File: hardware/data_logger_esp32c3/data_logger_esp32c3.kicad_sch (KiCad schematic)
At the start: 8 parts, among them J1 USB_C_Receptacle_USB2.0, U1 ESP32-C3-MINI-1

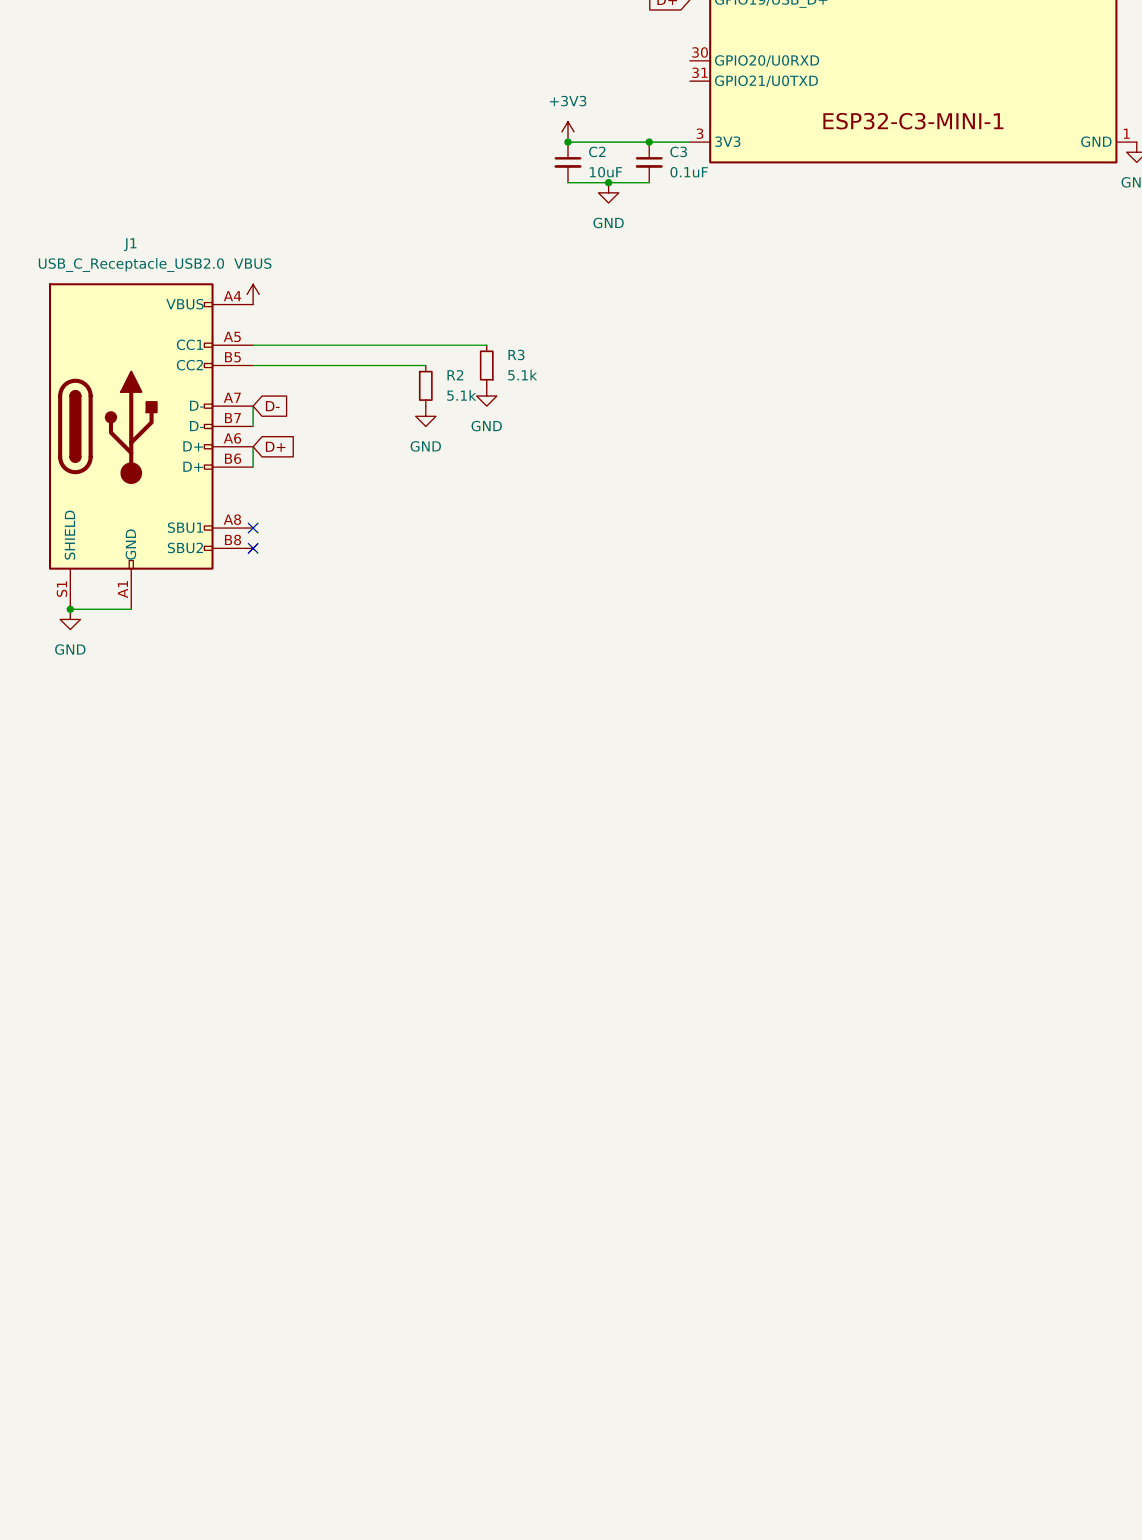
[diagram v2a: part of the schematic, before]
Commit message: Added regulator circuit
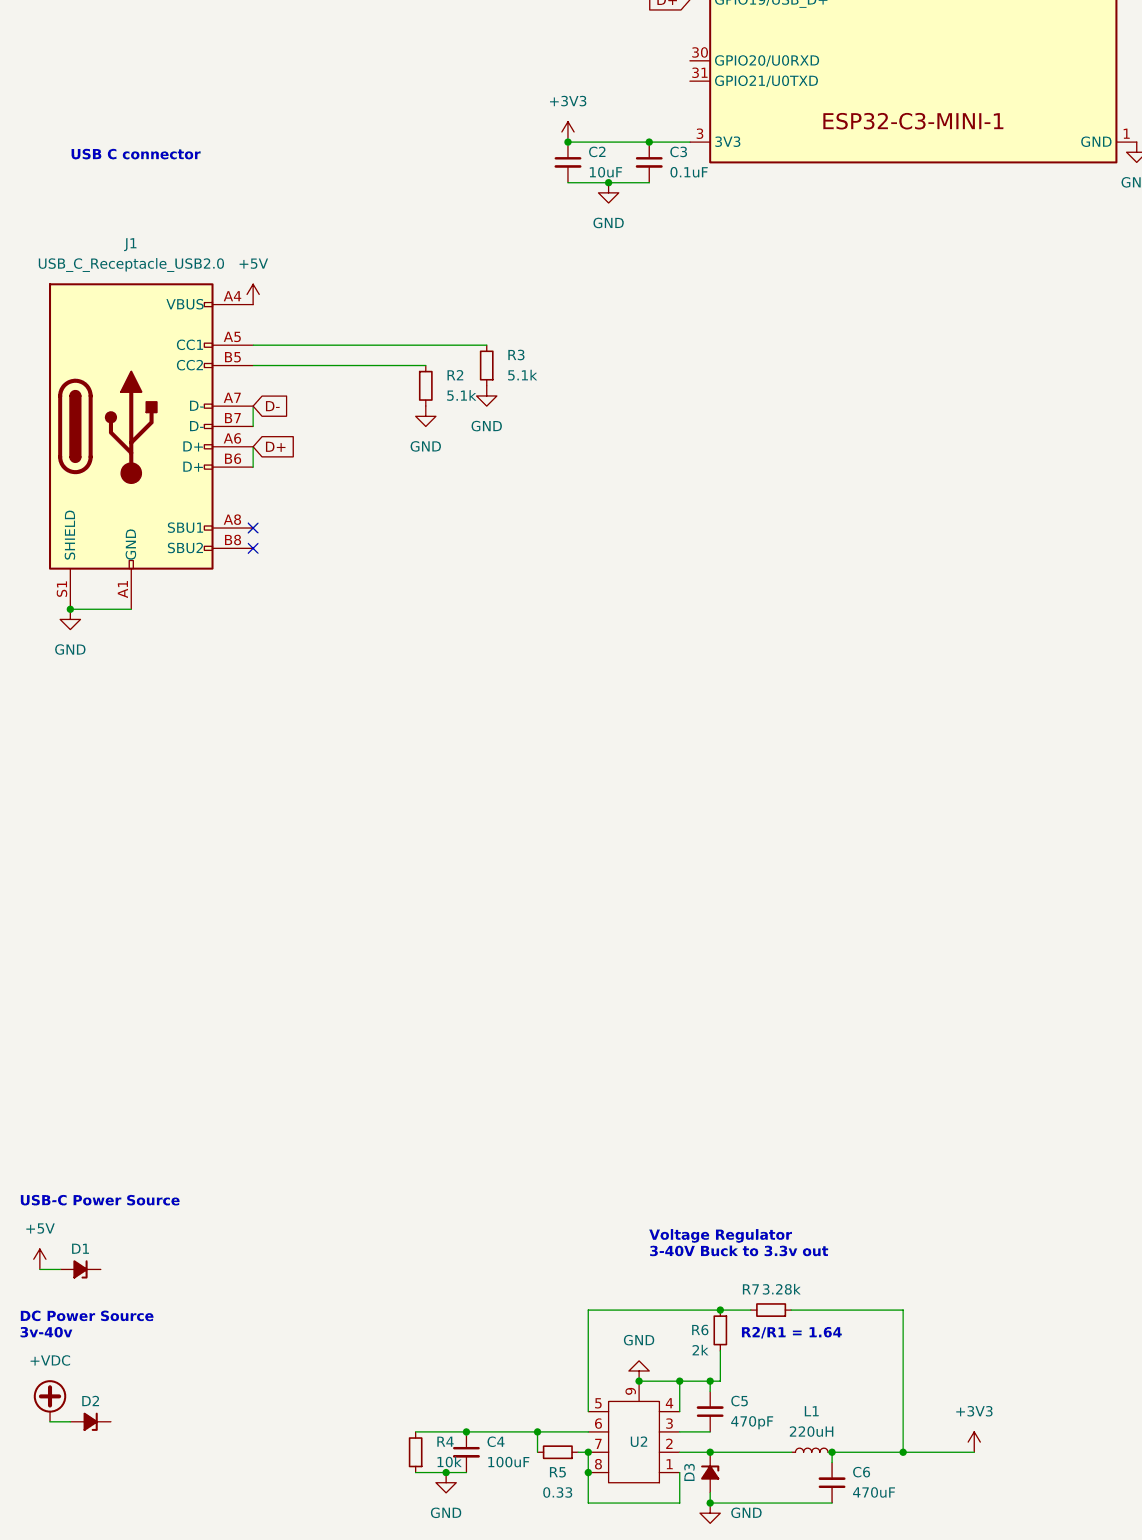
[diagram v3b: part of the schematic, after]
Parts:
- added C4: 100uF, Capacitor_SMD:C_0603_1608Metric, symbol Device:C_Small
- added C5: 470pF, Capacitor_SMD:C_0603_1608Metric, symbol Device:C_Small
- added C6: 470uF, Capacitor_SMD:C_0603_1608Metric, symbol Device:C_Small
- added D1, D2, D3: D_Zener_Small_Filled, Diode_SMD:D_0603_1608Metric, symbol Device:D_Zener_Small_Filled
- added L1: 220uH, Inductor_SMD:L_6.3x6.3_H3, symbol Device:L_Small
- added R4: 10k, Resistor_SMD:R_0603_1608Metric, symbol Device:R_Small
- added R5: 0.33, Resistor_SMD:R_0603_1608Metric, symbol Device:R_Small
- added R6: 2k, Resistor_SMD:R_0603_1608Metric, symbol Device:R_Small
- added R7: 3.28k, Resistor_SMD:R_0603_1608Metric, symbol Device:R_Small
- added U2: MC34063ADRJR, lib:8-WDFN Exposed Pad, symbol lib:MC34063ADRJR
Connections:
- net +3V3: now also C6.2, L1.2, R7.1
- net GND: now also C4.2, C5.2, C6.1, D3.2 (A), R4.1, R6.2, U2.4 (gnd), U2.9 (thermal_pad)
- net VBUS renamed +5V
- net +5V: now also D1.2 (A)
- new net: C4.1, R4.2, R5.2, U2.6 (Vcc)
- new net: R5.1, U2.1 (switch_collector), U2.7 (Ipk), U2.8 (drive_collector)
- new net: D3.1 (K), L1.1, U2.2 (switch_emitter)
- new net: C5.1, U2.3 (timing_cap)
- new net: R6.1, R7.2, U2.5 (comparitor_inverting_input)
- new net +VDC: D2.2 (A)
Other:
- note added: "DC Power Source 3v-40v"
- note added: "R2/R1 = 1.64"
- note added: "USB C connector"
- note added: "USB-C Power Source"
- note added: "Voltage Regulator 3-40V Buck to 3.3v out"

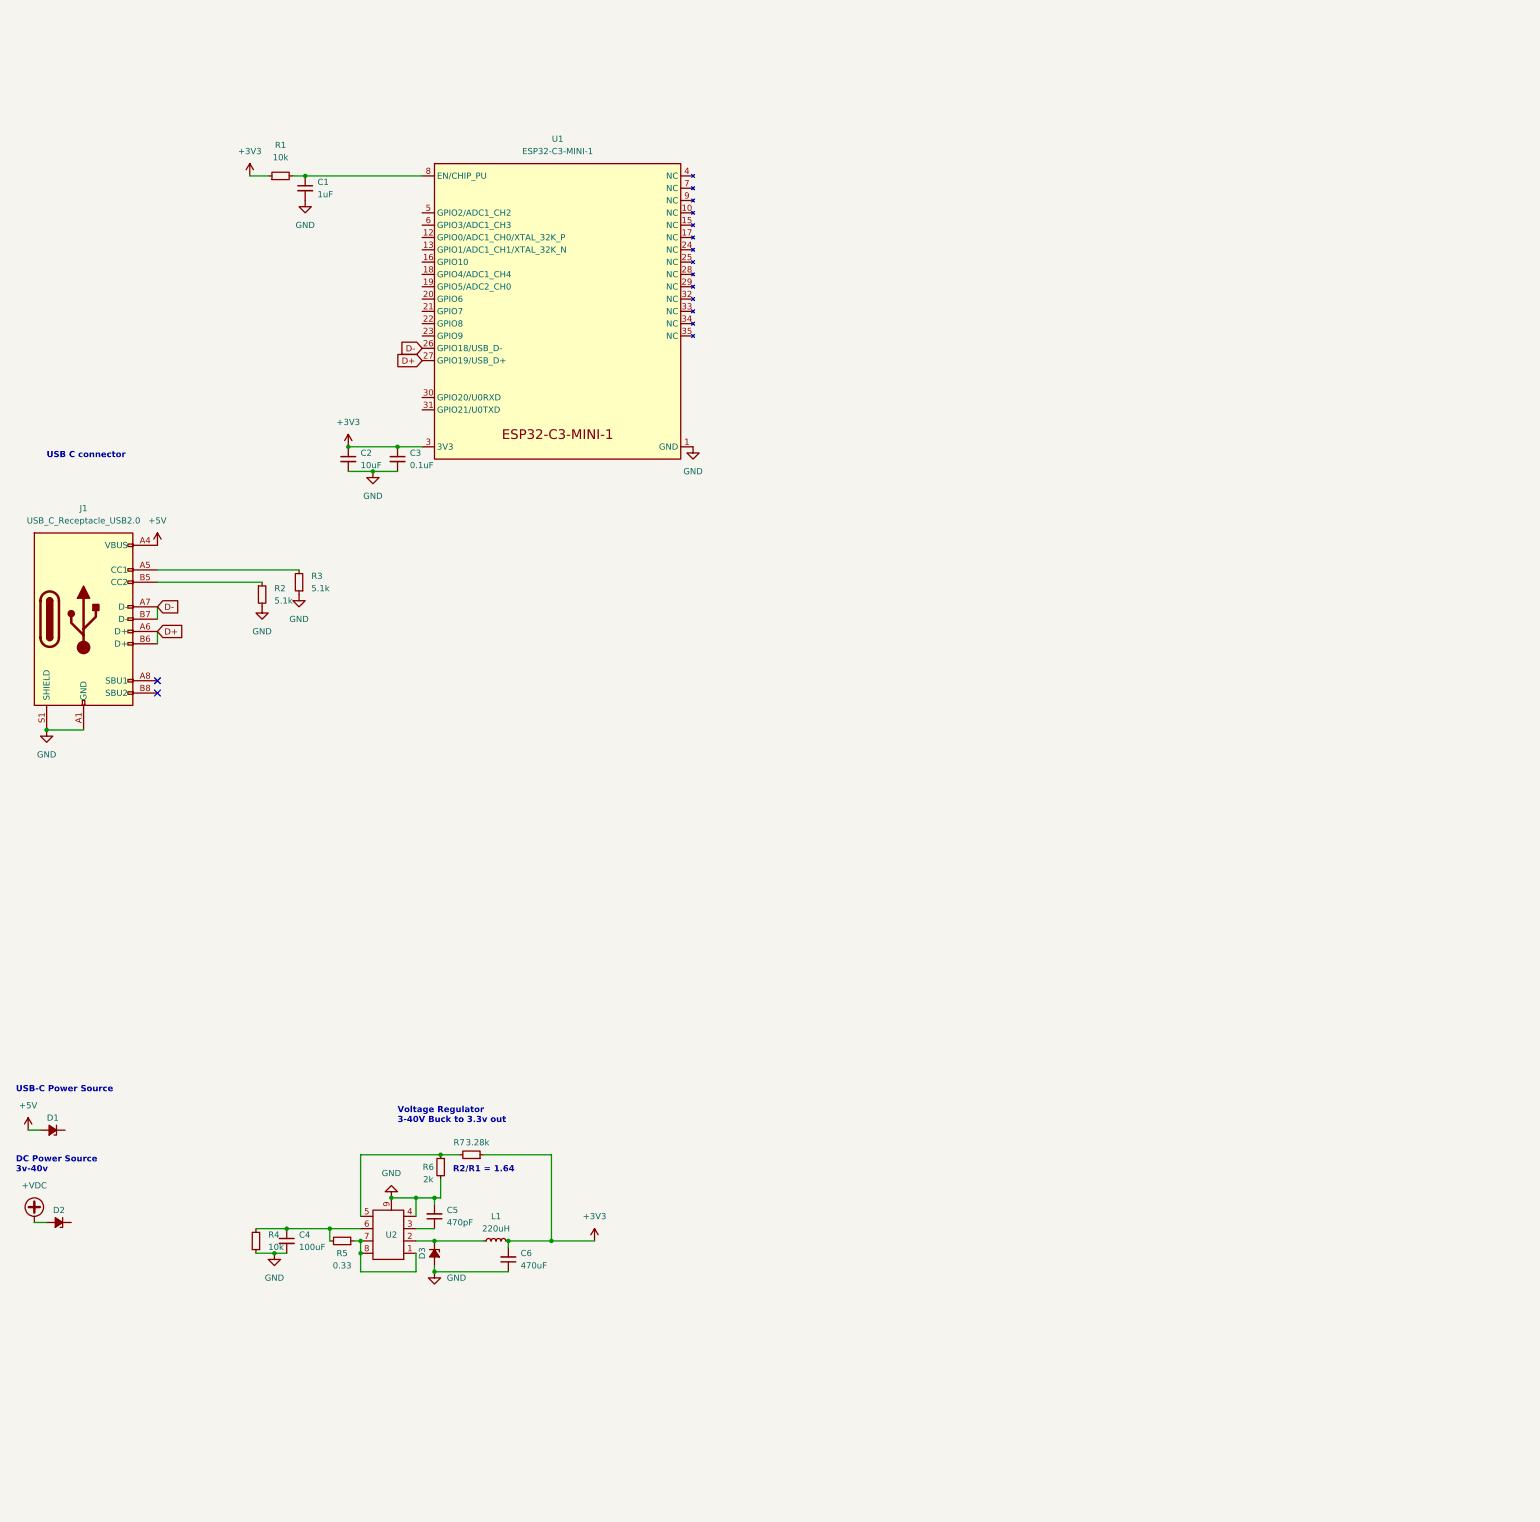
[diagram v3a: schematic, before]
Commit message: Added uSD circuit
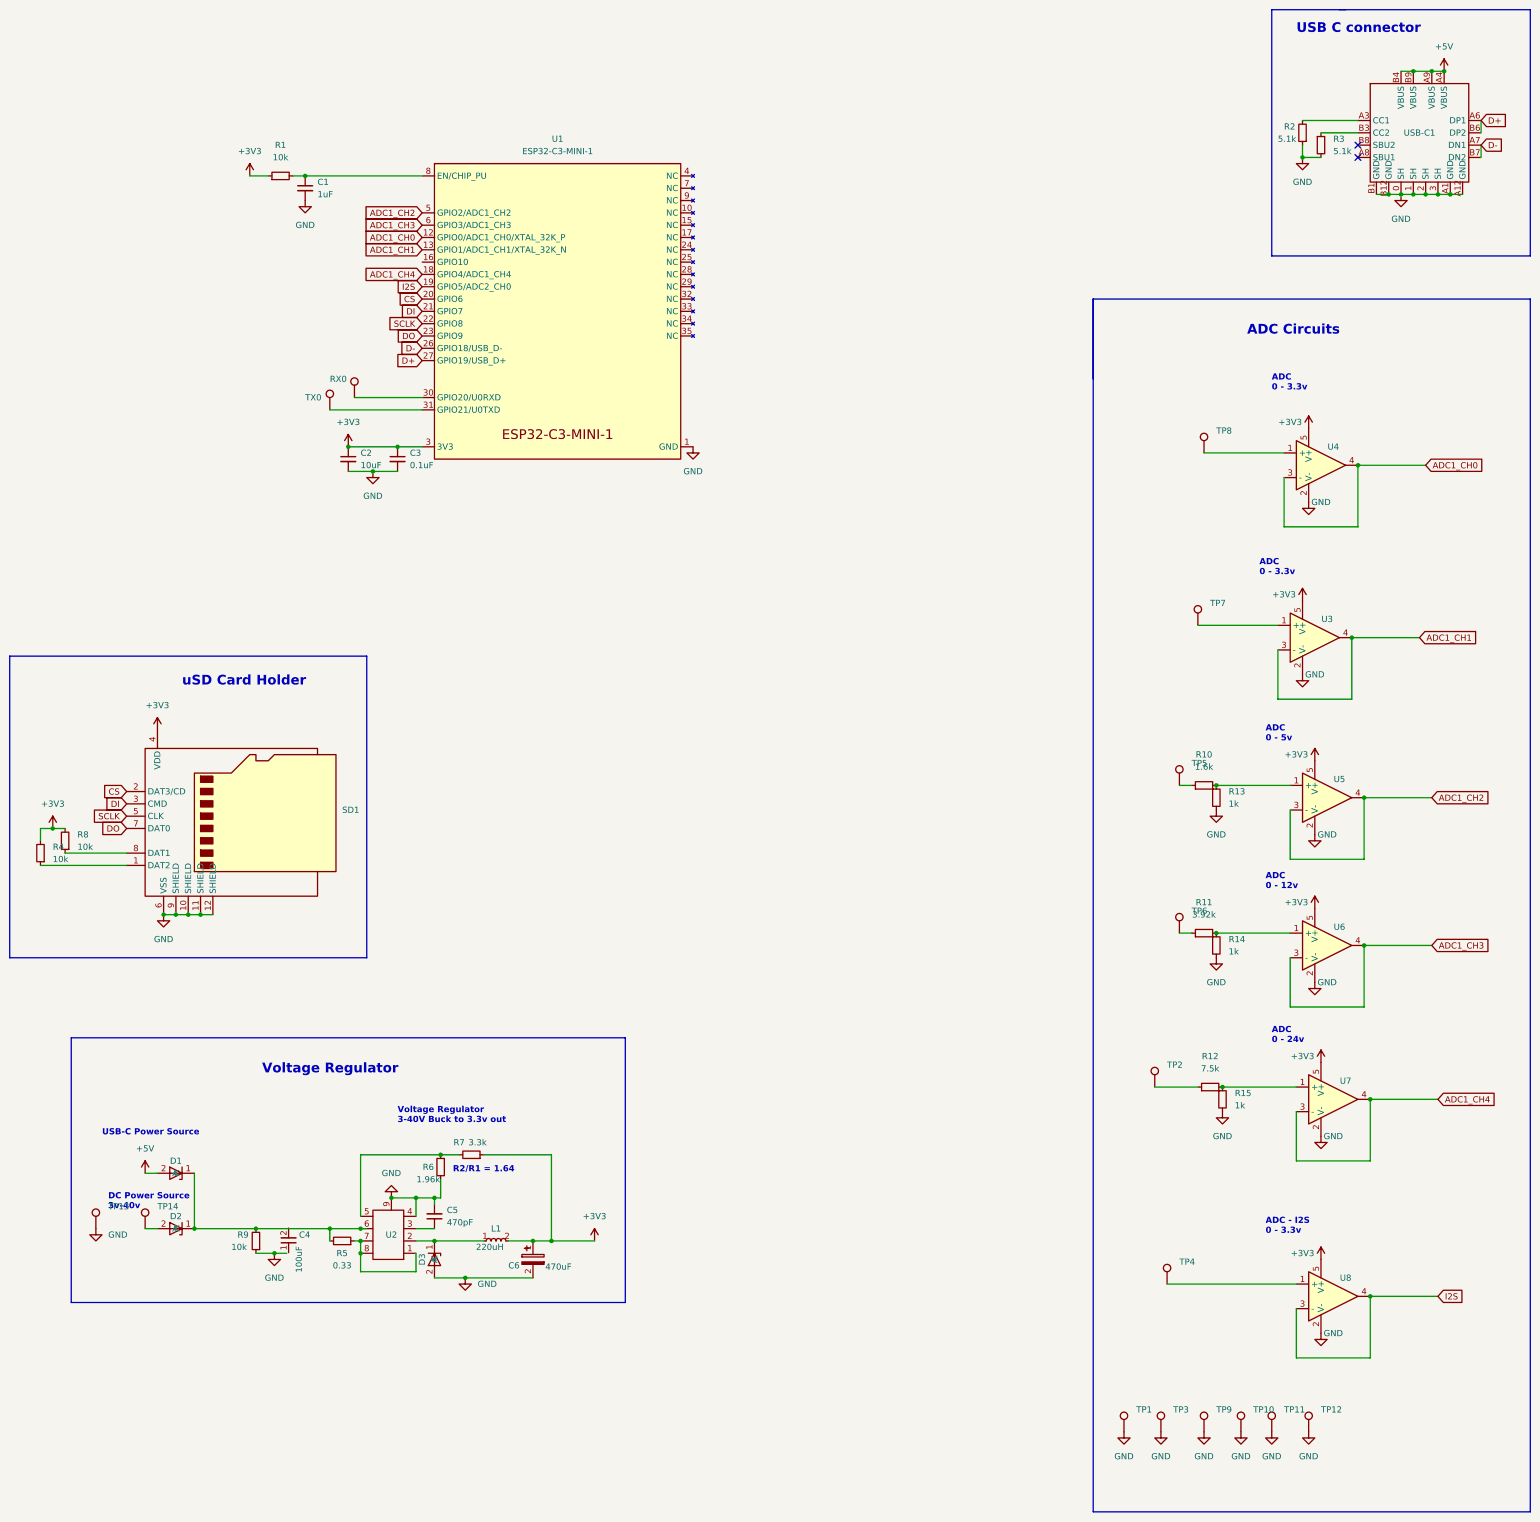
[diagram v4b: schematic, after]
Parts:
- removed C4: 100uF, Capacitor_SMD:C_0603_1608Metric, symbol Device:C_Small
- removed C6: 470uF, Capacitor_SMD:C_0603_1608Metric, symbol Device:C_Small
- removed D1, D2, D3: D_Zener_Small_Filled, Diode_SMD:D_0603_1608Metric, symbol Device:D_Zener_Small_Filled
- removed J1: USB_C_Receptacle_USB2.0, type_c:USB_C_GCT_USB4085, symbol Connector:USB_C_Receptacle_USB2.0
- removed L1: 220uH, Inductor_SMD:L_6.3x6.3_H3, symbol Device:L_Small
- added C4: 100uF, lib:RT1H101M0810, symbol lib:RT1H101M0810
- added C6: KF471M016F115A, lib:KF471M016F115A, symbol lib:KF471M016F115A
- added D1, D2, D3: B0530WS_SE, lib:B0530WS_SE, symbol lib:B0530WS_SE
- added L1: 220uH, lib:SMDRI127-221MT, symbol lib:SMDRI127-221MT
- added R10: 1.6k, Resistor_SMD:R_0603_1608Metric, symbol Device:R_Small
- added R11: 3.92k, symbol Device:R_Small
- added R12: 7.5k, Resistor_SMD:R_0603_1608Metric, symbol Device:R_Small
- added R13, R14, R15: 1k, Resistor_SMD:R_0603_1608Metric, symbol Device:R_Small
- added R8, R9: 10k, Resistor_SMD:R_0603_1608Metric, symbol Device:R_Small
- added RX0, TP1, TP10, TP11, TP12, TP13, TP14, TP2, TP3, TP4, TP5, TP6, TP7, TP8, TP9, TX0: TestPoint, TestPoint:TestPoint_Loop_D2.50mm_Drill1.0mm, symbol Connector:TestPoint
- added SD1: 472192001, lib:472192001, symbol lib:472192001
- added U3, U4, U5, U6, U7, U8: LM321MF, lib:LM321MF, symbol lib:LM321MF
- added USB-C1: USB-TYPE-C-018, lib:USB-TYPE-C-018, symbol lib:USB-TYPE-C-018
- C1: part_number (none) -> TMK107AB7105KAHT
- C2: part_number (none) -> GRM188R61A106ME69D
- C3: part_number (none) -> AC0603KRX7R9BB104
- C5: part_number (none) -> CC0603JRNPO9BN471
- R1, R4: part_number (none) -> AC0603FR-0710KL
- R2, R3: part_number (none) -> RC0603FR-075K1L
- R5: part_number (none) -> RL06FTNR330
- R6: value 2k -> 1.96k; part_number (none) -> RMS06FT1961
- R7: value 3.28k -> 3.3k; part_number (none) -> v
- U2: part_number (none) -> MC34063ADRJR
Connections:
- net +3V3: now also R4.2, C6.1, L1.2, R8.2, SD1.4 (VDD), U3.5 (V+), U4.5 (V+), U5.5 (V+), U6.5 (V+), U7.5 (V+), U8.5 (V+)
- net +5V: now also D1.2 (A), USB-C1.A4 (VBUS), USB-C1.A9 (VBUS), USB-C1.B4 (VBUS), USB-C1.B9 (VBUS)
- net D+: now also USB-C1.A6 (DP1), USB-C1.B6 (DP2)
- net D-: now also USB-C1.A7 (DN1), USB-C1.B7 (DN2)
- net GND: now also R2.1, R3.2, C6.2, D3.2 (A), R13.2, R14.2, R15.2, R9.1, SD1.10 (SHIELD), SD1.11 (SHIELD), SD1.12 (SHIELD), SD1.6 (VSS), SD1.9 (SHIELD), TP1.1, TP10.1, TP11.1, TP12.1, TP13.1, TP3.1, TP9.1, U3.2 (V-), U4.2 (V-), U5.2 (V-), U6.2 (V-), U7.2 (V-), U8.2 (V-), USB-C1.0 (SH), USB-C1.1 (SH), USB-C1.2 (SH), USB-C1.3 (SH), USB-C1.A1 (GND), USB-C1.A12 (GND), USB-C1.B1 (GND), USB-C1.B12 (GND); no longer R2.2, R3.1, R4.1
- net at R5.2, U2.6 (Vcc): now also D1.1 (K), D2.1 (K), R9.2; no longer R4.2
- net at U2.2 (switch_emitter): now also D3.1 (K), L1.1
- net ADC1_CH0: now reaches U1.12 (GPIO0/ADC1_CH0/XTAL_32K_P)
- net ADC1_CH0: now also U4.3 (-), U4.4
- net ADC1_CH1: now reaches U1.13 (GPIO1/ADC1_CH1/XTAL_32K_N)
- net ADC1_CH1: now also U3.3 (-), U3.4
- net ADC1_CH4: now reaches U1.18 (GPIO4/ADC1_CH4)
- net ADC1_CH4: now also U7.3 (-), U7.4
- net I2S: now reaches U1.19 (GPIO5/ADC2_CH0)
- net I2S: now also U8.3 (-), U8.4
- net CS: now reaches U1.20 (GPIO6)
- net CS: now also SD1.2 (DAT3/CD)
- net DI: now reaches U1.21 (GPIO7)
- net DI: now also SD1.3 (CMD)
- net SCLK: now reaches U1.22 (GPIO8)
- net SCLK: now also SD1.5 (CLK)
- net DO: now reaches U1.23 (GPIO9)
- net DO: now also SD1.7 (DAT0)
- net at U1.30 (GPIO20/U0RXD): now also RX0.1
- net at U1.31 (GPIO21/U0TXD): now also TX0.1
- net ADC1_CH2: now reaches U1.5 (GPIO2/ADC1_CH2)
- net ADC1_CH2: now also U5.3 (-), U5.4
- net ADC1_CH3: now reaches U1.6 (GPIO3/ADC1_CH3)
- net ADC1_CH3: now also U6.3 (-), U6.4
- new net: TP7.1, U3.1 (+)
- new net: R2.2, USB-C1.A3 (CC1)
- new net: R10.1, TP5.1
- new net: R10.2, R13.1, U5.1 (+)
- new net: R11.1, TP6.1
- new net: TP8.1, U4.1 (+)
- new net: R12.2, R15.1, U7.1 (+)
- new net: D2.2 (A), TP14.1
- new net: R12.1, TP2.1
- new net: R3.1, USB-C1.B3 (CC2)
- new net: R11.2, R14.1, U6.1 (+)
- new net: R4.1, SD1.1 (DAT2)
- new net: R8.1, SD1.8 (DAT1)
- new net: TP4.1, U8.1 (+)
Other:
- note added: "ADC - I2S 0 - 3.3v"
- note added: "ADC 0 - 12v"
- note added: "ADC 0 - 24v"
- note added: "ADC 0 - 3.3v"
- note added: "ADC 0 - 5v"
- note added: "ADC Circuits"
- note added: "Voltage Regulator"
- note added: "uSD Card Holder"
